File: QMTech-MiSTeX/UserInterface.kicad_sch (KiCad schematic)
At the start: 75 parts, among them CN1 PJ-325C5-BL, CN2 U.FL-R-SMT-1(80), CN3 U.FL-R-SMT-1(80), CN4 U.FL-R-SMT-1(80), CN5 U.FL-R-SMT-1(80), SW1 TS-1187A-B-A-B, SW2 TS-1187A-B-A-B, SW3 TS-1187A-B-A-B, SW4 TS-1187A-B-A-B, SW5 XKB5858-W-F-75, SW6 XKB5858-W-F-75, SW7 DSHP04TSGER, U5 ZGY133/T10(PLT)

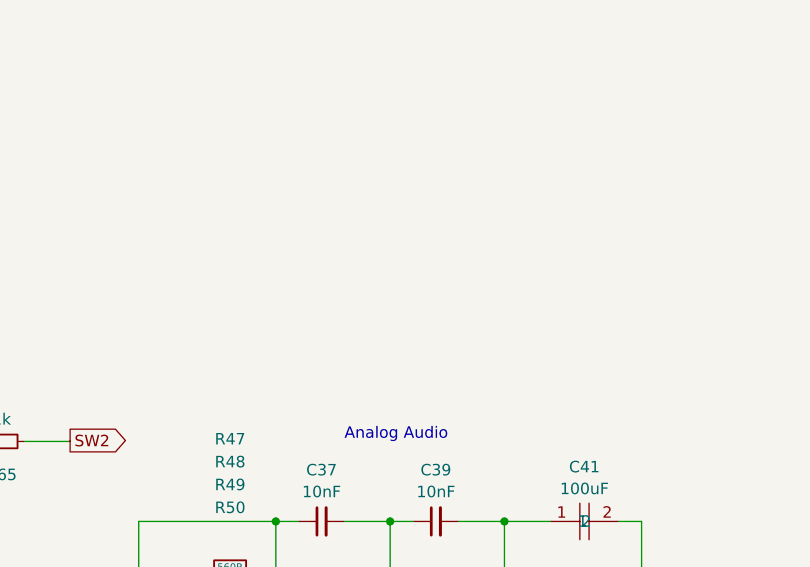
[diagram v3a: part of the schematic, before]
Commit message: Add ESD protection to headphone jack and Pmod
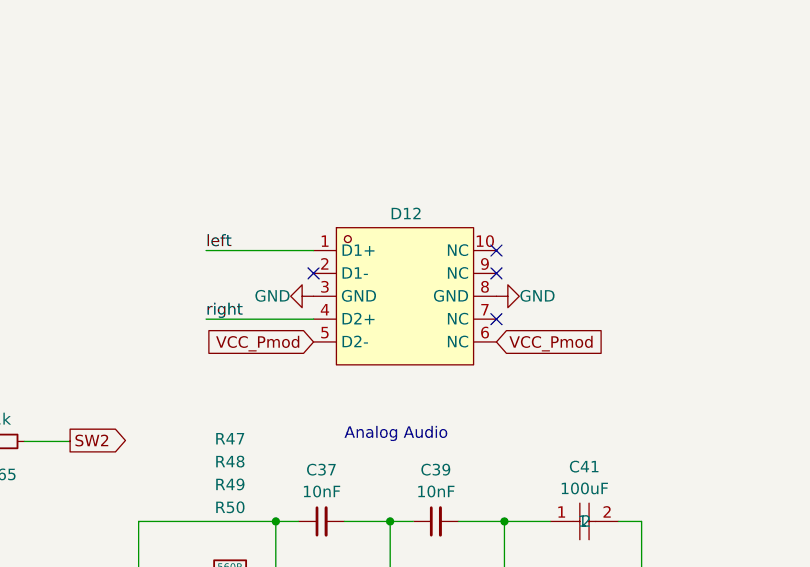
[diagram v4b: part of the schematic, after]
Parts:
- added D12: TPD4E05U06DQAR_C2972498, easyeda2kicad:DFN2510-10_L2.5-W1.0-P0.50-BL, symbol easyeda2kicad:TPD4E05U06DQAR_C2972498
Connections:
- net GND: now also D12.3 (GND), D12.8 (GND)
- net left: now also D12.1 (D1+)
- net right: now also D12.4 (D2+)
- new net VCC_Pmod: D12.5 (D2-), D12.6 (NC)
- no-connect marks 10 -> 14
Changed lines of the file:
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@@
   (no_connect (at 250.8504 152.8572))
   (no_connect (at 110.49 124.46))
+  (no_connect (at 215.011 113.411))
   (no_connect (at 147.32 130.7099))
   (no_connect (at 157.48 130.7099))
   (no_connect (at 74.295 57.785))
+  (no_connect (at 215.011 115.951))
   (no_connect (at 127 144.78))
+  (no_connect (at 215.011 121.031))
   (no_connect (at 94.615 57.785))
   (no_connect (at 110.49 121.92))
   (no_connect (at 250.8504 154.1272))
   (no_connect (at 137.16 144.78))
+  (no_connect (at 194.691 115.951))
   (wire (pts (xy 47.5488 164.2618) (xy 47.2948 164.2618))
     (stroke (width 0) (type default))
@@
     (stroke (width 0) (type default))
   )
+  (wire (pts (xy 182.753 113.411) (xy 194.691 113.411))
+    (stroke (width 0.254) (type default))
+  )
   (wire (pts (xy 100.4486 134.5184) (xy 93.4677 134.5184))
     (stroke (width 0) (type default))
@@
     (stroke (width 0) (type default))
   )
+  (wire (pts (xy 182.753 121.031) (xy 194.691 121.031))
+    (stroke (width 0.254) (type default))
+  )
   (wire (pts (xy 115.57 76.2) (xy 115.57 88.9))
     (stroke (width 0) (type default))
@@
     (effects (font (size 1.27 1.27)) (justify left bottom))
   )
+  (label "right" (at 182.753 121.031 180) (fields_autoplaced)
+    (effects (font (size 1.27 1.27)) (justify left bottom))
+  )
   (label "SNAC1" (at 53.1945 60.96 180) (fields_autoplaced)
     (effects (font (size 1.27 1.27)) (justify right bottom))
@@
     (effects (font (size 1.27 1.27)) (justify left bottom))
   )
+  (label "left" (at 182.753 113.411 180) (fields_autoplaced)
+    (effects (font (size 1.27 1.27)) (justify left bottom))
+  )
   (label "SNAC6" (at 25.4966 105.7123 0) (fields_autoplaced)
     (effects (font (size 1.27 1.27)) (justify left bottom))
@@
     )
   )
+  (global_label "VCC_Pmod" (shape input) (at 215.011 123.571 0) (fields_autoplaced)
+    (effects (font (size 1.27 1.27)) (justify left))
+    (property "Intersheetrefs" "${INTERSHEET_REFS}" (at 227.9488 123.571 0)
+      (effects (font (size 1.27 1.27)) (justify left))
+    )
+  )
   (global_label "BTN_USER" (shape output) (at 47.5488 164.2618 0) (fields_autoplaced)
     (effects (font (size 1.27 1.27)) (justify left))
@@
     )
   )
+  (global_label "VCC_Pmod" (shape input) (at 194.691 123.571 180) (fields_autoplaced)
+    (effects (font (size 1.27 1.27)) (justify right))
+    (property "Intersheetrefs" "${INTERSHEET_REFS}" (at 181.7532 123.571 0)
+      (effects (font (size 1.27 1.27)) (justify right))
+    )
+  )
   (symbol (lib_id "Connector:TestPoint_Flag") (at 253.9238 59.0804 0) (unit 1)
     (in_bom yes) (on_board yes) (dnp no) (fields_autoplaced)
@@
     )
   )
+  (symbol (lib_id "easyeda2kicad:TPD4E05U06DQAR_C2972498") (at 206.121 118.491 0) (unit 1)
+    (in_bom yes) (on_board yes) (dnp no)
+    (property "Reference" "D12" (at 204.978 109.347 0)
+      (effects (font (size 1.27 1.27)))
+    )
+    (property "Value" "TPD4E05U06DQAR_C2972498" (at 204.851 109.2779 0)
+      (effects (font (size 1.27 1.27)) hide)
+    )
+    (property "Footprint" "easyeda2kicad:DFN2510-10_L2.5-W1.0-P0.50-BL" (at 206.121 131.191 0)
+      (effects (font (size 1.27 1.27)) hide)
+    )
+    (property "Datasheet" "" (at 206.121 118.491 0)
+      (effects (font (size 1.27 1.27)) hide)
+    )
+    (property "LCSC Part" "C2972498" (at 206.121 133.731 0)
+      (effects (font (size 1.27 1.27)) hide)
+    )
+    (pin "7")
+    (pin "8")
+    (pin "2")
+    (pin "4")
+    (pin "3")
+    (pin "6")
+    (pin "5")
+    (pin "10")
+    (pin "1")
+    (pin "9")
+    (instances
+      (project "QMTech-MiSTeX"
+        (path "/bf95850e-2fcb-4784-a603-f17fc357556b/cce2b405-ae09-44af-ba42-d113d6ffe521"
+          (reference "D12") (unit 1)
+        )
+      )
+    )
+  )
   (symbol (lib_id "jlcpcb-basic-led:D_LED_0805_White") (at 64.0334 120.4214 90) (unit 1)
     (in_bom yes) (on_board yes) (dnp no) (fields_autoplaced)
@@
     )
   )
+  (symbol (lib_id "power:GND") (at 194.691 118.491 270) (unit 1)
+    (in_bom yes) (on_board yes) (dnp no)
+    (property "Reference" "#PWR0193" (at 188.341 118.491 0)
+      (effects (font (size 1.27 1.27)) hide)
+    )
+    (property "Value" "GND" (at 190.1284 118.491 90)
+      (effects (font (size 1.27 1.27)))
+    )
+    (property "Footprint" "" (at 194.691 118.491 0)
+      (effects (font (size 1.27 1.27)) hide)
+    )
+    (property "Datasheet" "" (at 194.691 118.491 0)
+      (effects (font (size 1.27 1.27)) hide)
+    )
+    (pin "1")
+    (instances
+      (project "QMTech-MiSTeX"
+        (path "/bf95850e-2fcb-4784-a603-f17fc357556b/cce2b405-ae09-44af-ba42-d113d6ffe521"
+          (reference "#PWR0193") (unit 1)
+        )
+      )
+    )
+  )
   (symbol (lib_id "easyeda2kicad:U.FL-R-SMT-1(80)") (at 127.2032 36.5506 270) (unit 1)
     (in_bom yes) (on_board yes) (dnp no) (fields_autoplaced)
@@
         )
       )
+    )
+  )
+  (symbol (lib_id "power:GND") (at 215.011 118.491 90) (unit 1)
+    (in_bom yes) (on_board yes) (dnp no)
+    (property "Reference" "#PWR0192" (at 221.361 118.491 0)
+      (effects (font (size 1.27 1.27)) hide)
+    )
+    (property "Value" "GND" (at 219.5736 118.491 90)
+      (effects (font (size 1.27 1.27)))
+    )
+    (property "Footprint" "" (at 215.011 118.491 0)
+      (effects (font (size 1.27 1.27)) hide)
+    )
+    (property "Datasheet" "" (at 215.011 118.491 0)
+      (effects (font (size 1.27 1.27)) hide)
+    )
+    (pin "1")
+    (instances
+      (project "QMTech-MiSTeX"
+        (path "/bf95850e-2fcb-4784-a603-f17fc357556b/cce2b405-ae09-44af-ba42-d113d6ffe521"
+          (reference "#PWR0192") (unit 1)
+        )
+      )

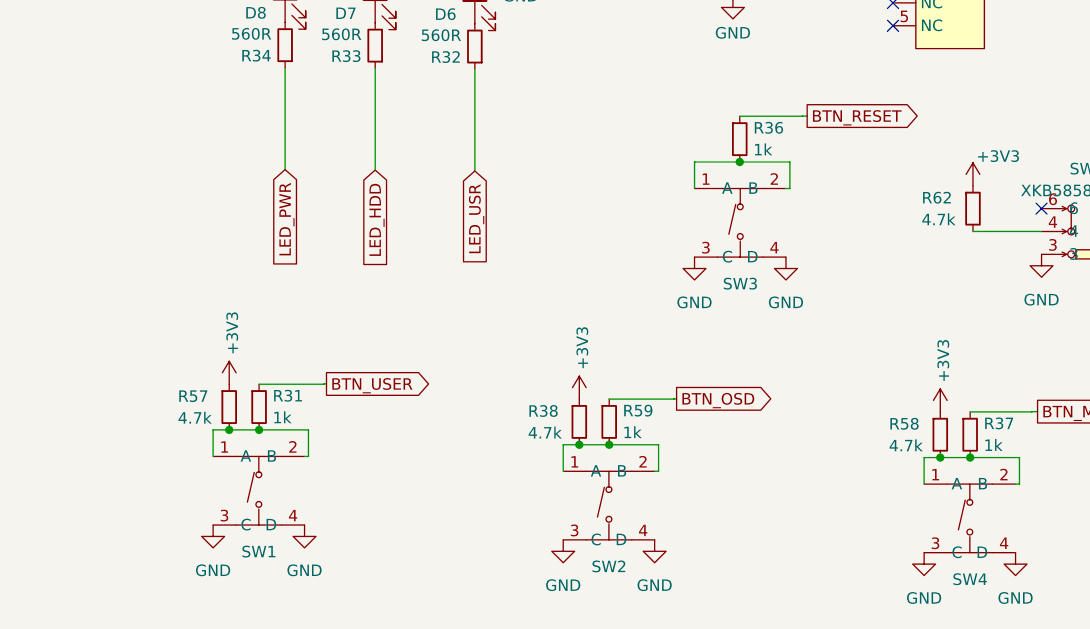
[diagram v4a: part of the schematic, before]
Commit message: add pin headers for buttons, add LED to RP2040, break out ADCs
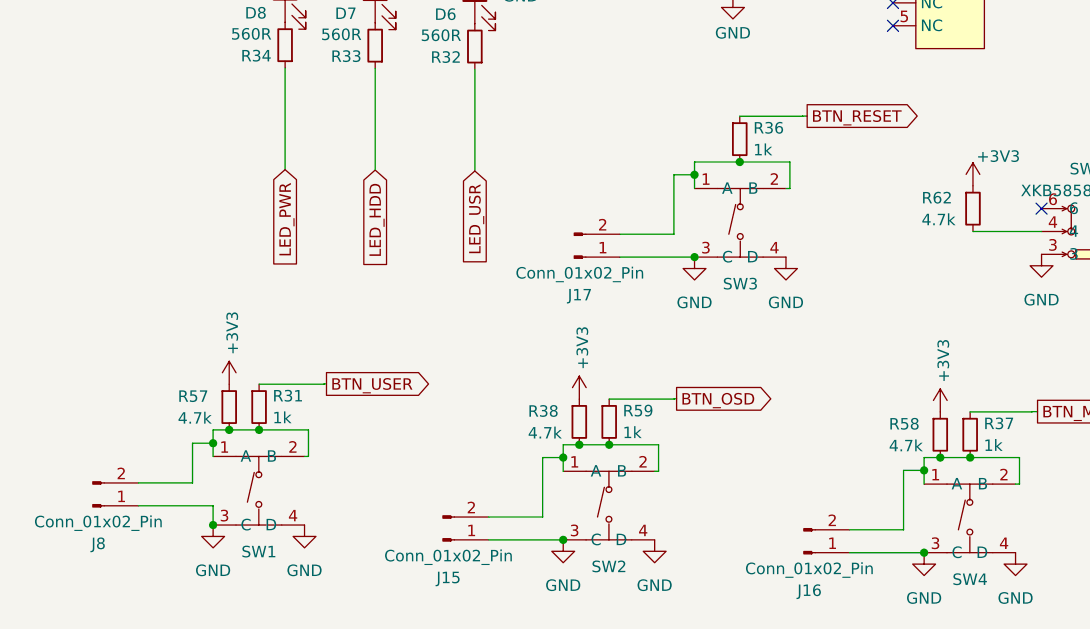
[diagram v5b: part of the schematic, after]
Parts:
- added J15, J16, J17, J8: Conn_01x02_Pin, Connector_PinHeader_2.54mm:PinHeader_1x02_P2.54mm_Vertical, symbol Connector:Conn_01x02_Pin
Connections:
- net GND: now also J15.1 (Pin_1), J16.1 (Pin_1), J17.1 (Pin_1), J8.1 (Pin_1)
- net at R38.2, R59.2, SW2.1 (A)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: now also J15.2 (Pin_2)
- net at R37.2, R58.2, SW4.1 (A)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: now also J16.2 (Pin_2)
- net at R31.2, R57.2, SW1.1 (A)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: now also J8.2 (Pin_2)
- net at R36.2, SW3.1 (A), SW3.2 (B): now also J17.2 (Pin_2)

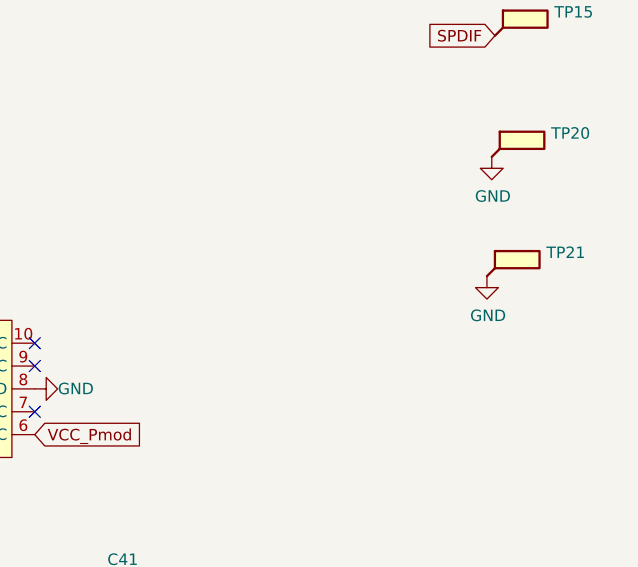
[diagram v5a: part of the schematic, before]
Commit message: add ground pin near USB test points, add GND vias to rp2040 center pad
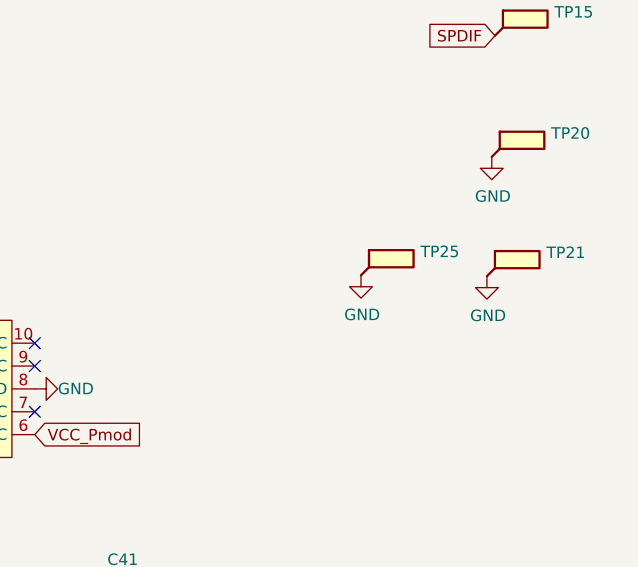
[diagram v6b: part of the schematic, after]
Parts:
- added TP25: TestPoint_Flag, TestPoint:TestPoint_Pad_D1.5mm, symbol Connector:TestPoint_Flag
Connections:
- net GND: now also TP25.1
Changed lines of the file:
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@@
+    )
+  )
+  (symbol (lib_id "power:GND") (at 251.2568 105.8672 0) (unit 1)
+    (in_bom yes) (on_board yes) (dnp no)
+    (property "Reference" "#PWR0199" (at 251.2568 112.2172 0)
+      (effects (font (size 1.27 1.27)) hide)
+    )
+    (property "Value" "GND" (at 251.3838 110.2614 0)
+      (effects (font (size 1.27 1.27)))
+    )
+    (property "Footprint" "" (at 251.2568 105.8672 0)
+      (effects (font (size 1.27 1.27)) hide)
+    )
+    (property "Datasheet" "" (at 251.2568 105.8672 0)
+      (effects (font (size 1.27 1.27)) hide)
+    )
+    (pin "1")
+    (instances
+      (project "QMTech-MiSTeX"
+        (path "/bf95850e-2fcb-4784-a603-f17fc357556b/cce2b405-ae09-44af-ba42-d113d6ffe521"
+          (reference "#PWR0199") (unit 1)
+        )
+      )
     )
   )
@@
         )
       )
+    )
+  )
+  (symbol (lib_id "Connector:TestPoint_Flag") (at 251.2568 105.8672 0) (unit 1)
+    (in_bom yes) (on_board yes) (dnp no) (fields_autoplaced)
+    (property "Reference" "TP25" (at 257.8608 103.2581 0)
+      (effects (font (size 1.27 1.27)) (justify left))
+    )
+    (property "Value" "TestPoint_Flag" (at 257.8608 105.6823 0)
+      (effects (font (size 1.27 1.27)) (justify left) hide)
+    )
+    (property "Footprint" "TestPoint:TestPoint_Pad_D1.5mm" (at 256.3368 105.8672 0)
+      (effects (font (size 1.27 1.27)) hide)
+    )
+    (property "Datasheet" "~" (at 256.3368 105.8672 0)
+      (effects (font (size 1.27 1.27)) hide)
+    )
+    (pin "1")
+    (instances
+      (project "QMTech-MiSTeX"
+        (path "/bf95850e-2fcb-4784-a603-f17fc357556b/cce2b405-ae09-44af-ba42-d113d6ffe521"
+          (reference "TP25") (unit 1)
+        )
+      )
